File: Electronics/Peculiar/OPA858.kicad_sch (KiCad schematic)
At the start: 12 parts, among them U15 ${SIM.PARAMS}, U18 ${SIM.PARAMS}

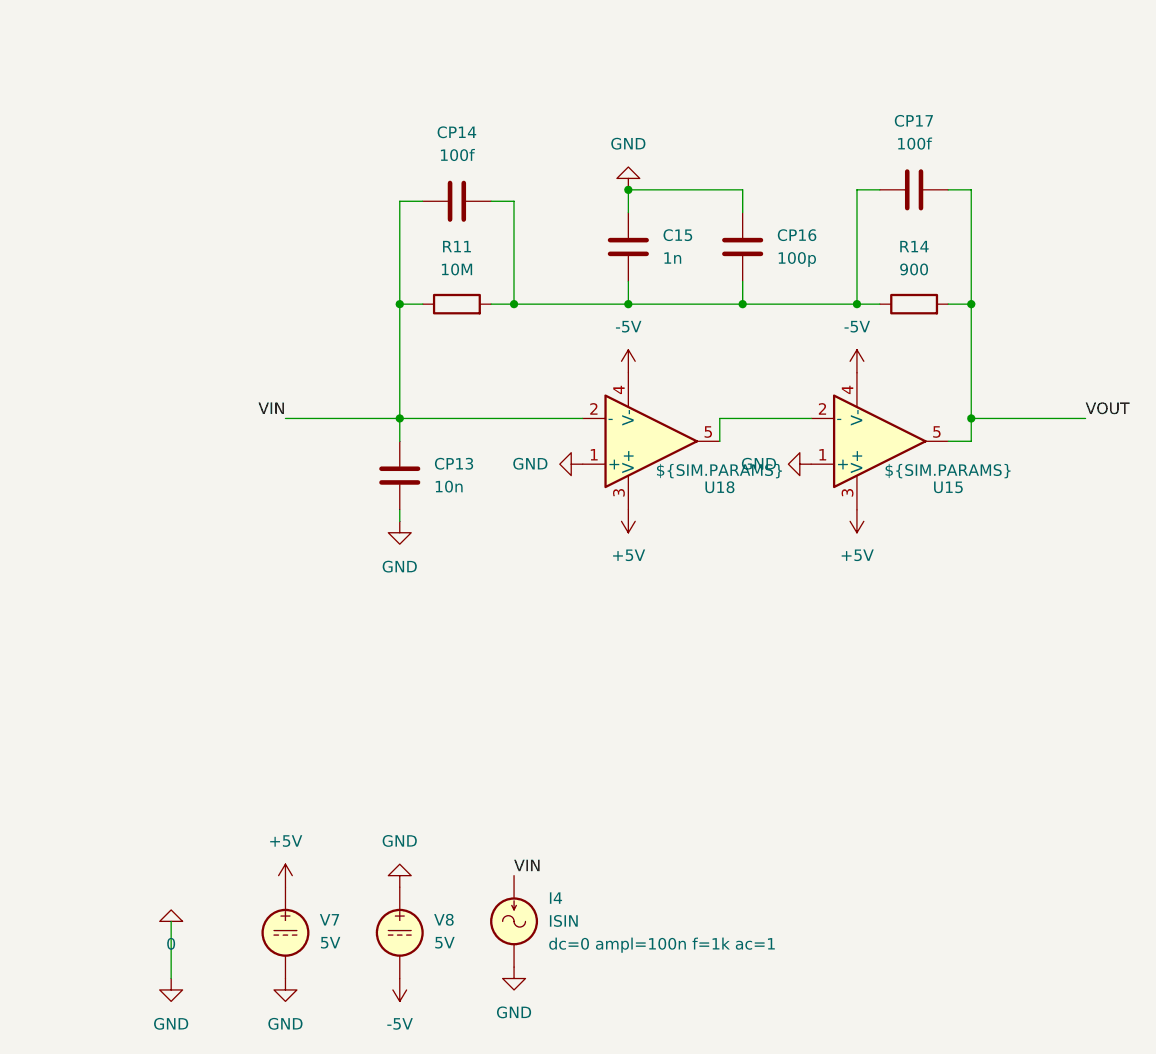
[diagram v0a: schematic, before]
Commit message: Separate two and three OPA858 designs
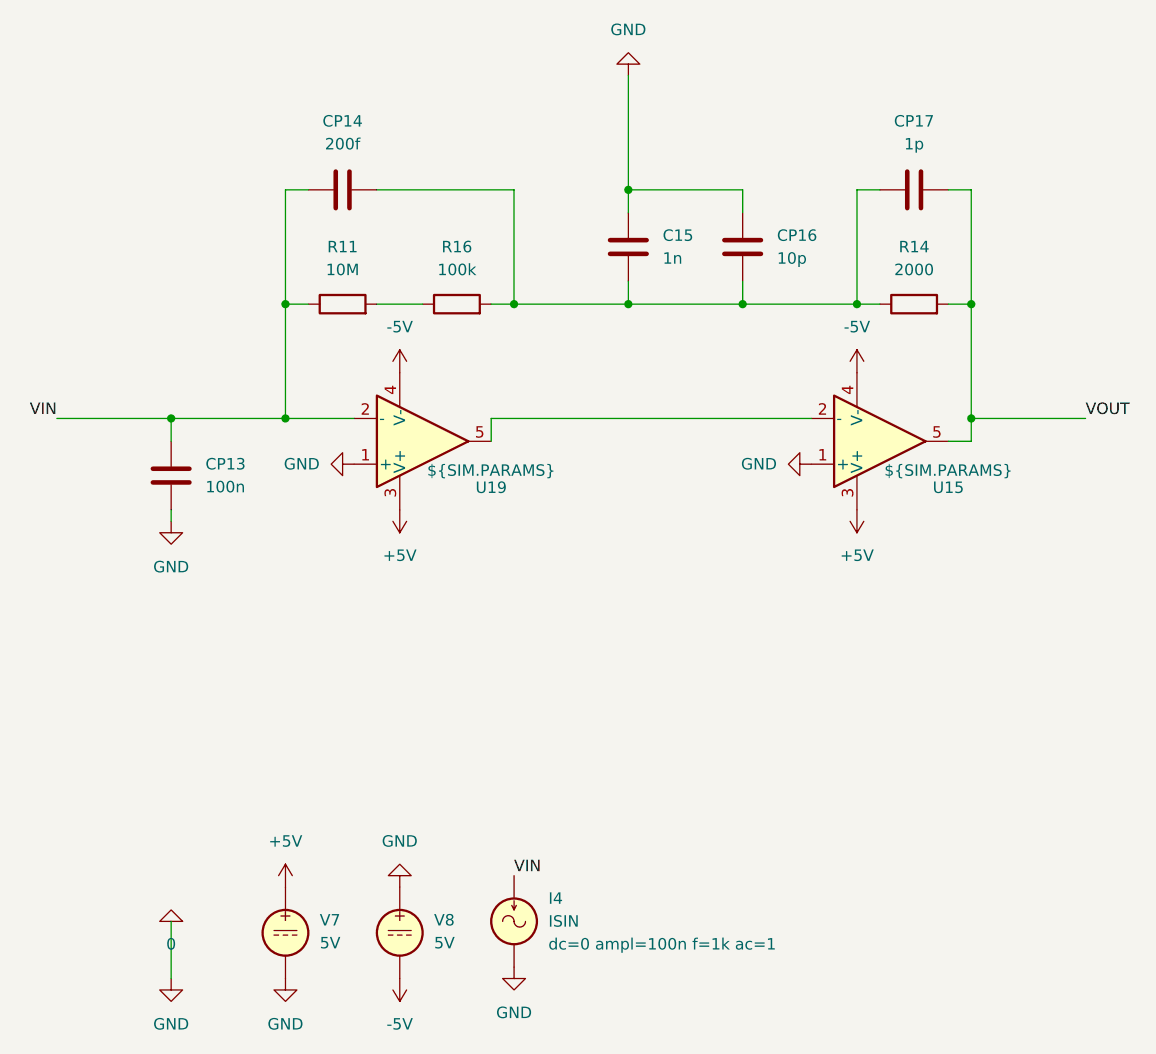
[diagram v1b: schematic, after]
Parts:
- removed U18: ${SIM.PARAMS}, symbol Simulation_SPICE:OPAMP
- added R16: 100k, symbol Device:R
- added U19: ${SIM.PARAMS}, symbol Simulation_SPICE:OPAMP
- CP13: value 10n -> 100n
- CP14: value 100f -> 200f
- CP16: value 100p -> 10p
- CP17: value 100f -> 1p
- R14: value 900 -> 2000
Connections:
- net +5V: now also U19.3 (V+)
- net -5V: now also U19.4 (V-)
- net 0: now also U19.1 (+)
- net VIN: now also U19.2 (-)
- net at C15.1, CP14.2, CP16.1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: now also R16.2; no longer R11.2
- net at U15.2 (-): now also U19.5
- new net: R11.2, R16.1
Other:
- moved on the sheet: CP13, CP14, R11
